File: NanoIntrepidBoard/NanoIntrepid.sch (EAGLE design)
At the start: 22 parts, among them Q1 TRANS_NPN, Q2 TRANS_NPN, Q3 TRANS_NPN, Q4 TRANS_PNP, Q5 TRANS_PNP, Q6 TRANS_PNP, U1 NANO, U2 MOSFET_P, U3 MOSFET_P, U4 MOSFET_P

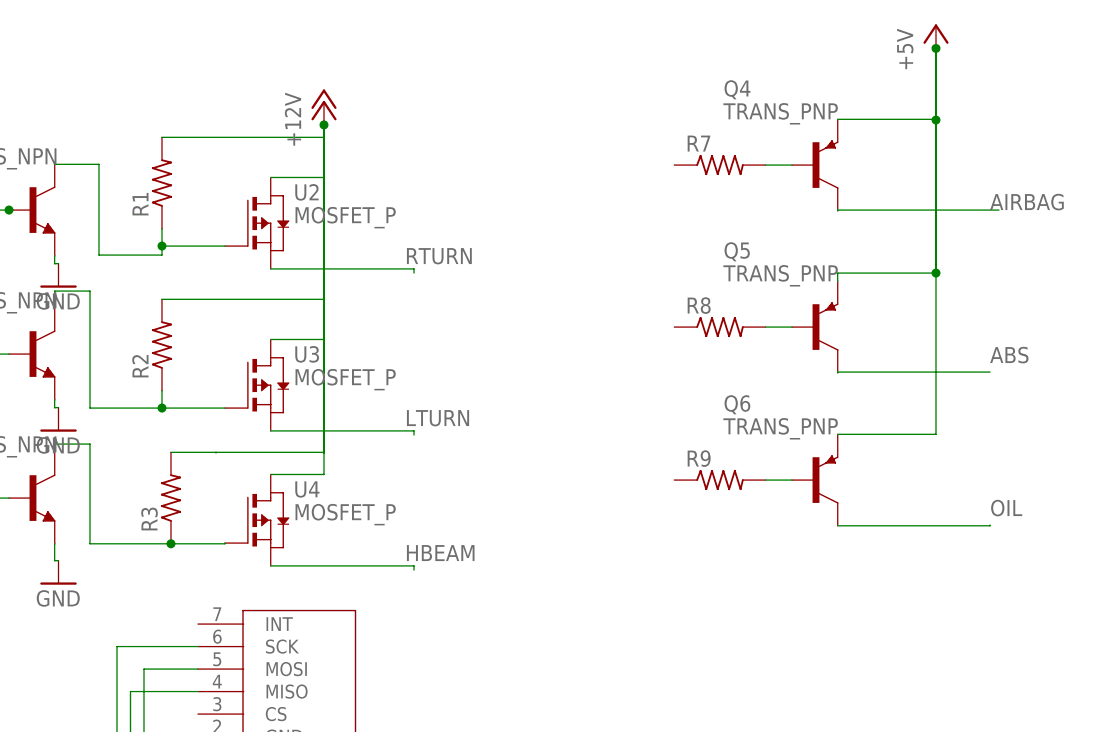
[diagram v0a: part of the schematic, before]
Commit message: Fixed some Eagle Library mistakes and started laying out board
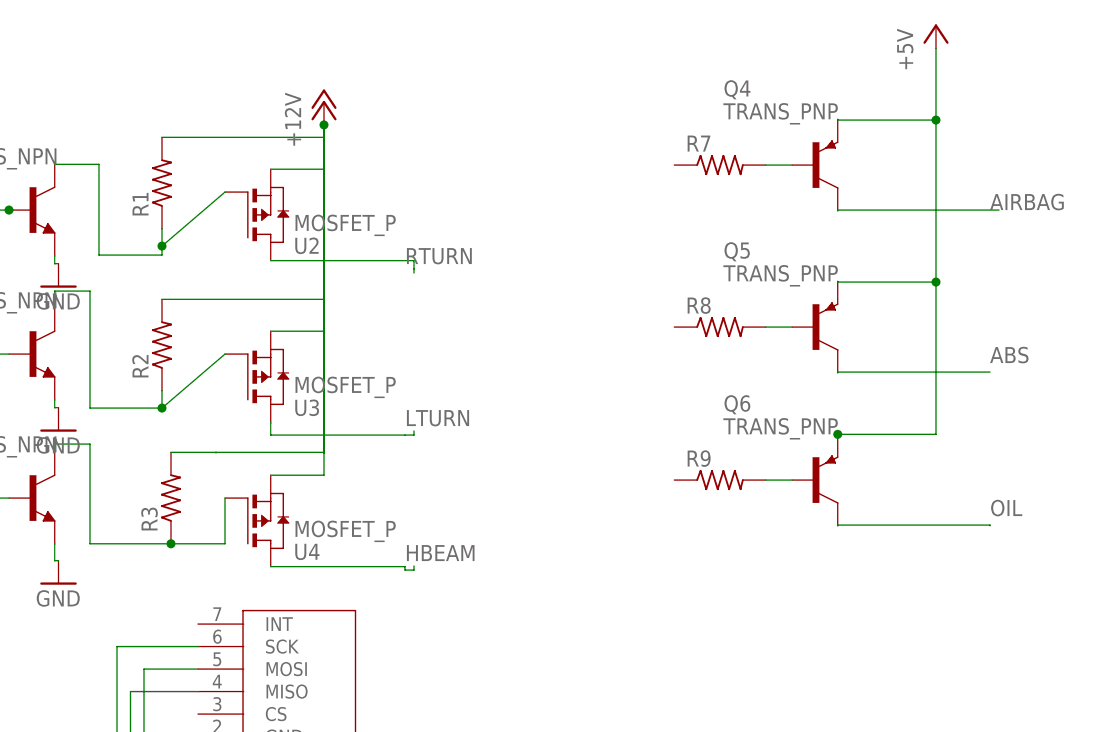
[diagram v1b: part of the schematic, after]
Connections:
- net +12V: now also U2.S, U3.S, U4.S; no longer U2.D, U3.D, U4.D
- net +5V: now also Q4.E, Q5.E, Q6.E; no longer Q4.C, Q5.C, Q6.C
- net ABS: now also Q5.C; no longer Q5.E
- net AIRBAG: now also Q4.C; no longer Q4.E
- net HBEAM: now also U4.D; no longer U4.S
- net LTURN: now also U3.D; no longer U3.S
- net OIL: now also Q6.C; no longer Q6.E
- net RTURN: now also U2.D; no longer U2.S
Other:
- moved on the sheet: U2, U3, U4
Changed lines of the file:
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@@
 <attribute name="VALUE" x="4.96" y="68.46" size="1.778" layer="96"/>
 </instance>
-<instance part="U2" gate="G$1" x="107" y="100" smashed="yes">
-<attribute name="VALUE" x="114.62" y="102.54" size="1.778" layer="96"/>
-<attribute name="NAME" x="114.62" y="105.08" size="1.778" layer="95"/>
-</instance>
-<instance part="U3" gate="G$1" x="107" y="82" smashed="yes">
-<attribute name="VALUE" x="114.62" y="84.54" size="1.778" layer="96"/>
-<attribute name="NAME" x="114.62" y="87.08" size="1.778" layer="95"/>
-</instance>
-<instance part="U4" gate="G$1" x="107" y="67" smashed="yes">
-<attribute name="VALUE" x="114.62" y="69.54" size="1.778" layer="96"/>
-<attribute name="NAME" x="114.62" y="72.08" size="1.778" layer="95"/>
+<instance part="U2" gate="G$1" x="107" y="106" smashed="yes" rot="MR180">
+<attribute name="VALUE" x="114.62" y="103.46" size="1.778" layer="96" rot="MR180"/>
+<attribute name="NAME" x="114.62" y="100.92" size="1.778" layer="95" rot="MR180"/>
+</instance>
+<instance part="U3" gate="G$1" x="107" y="88" smashed="yes" rot="MR180">
+<attribute name="VALUE" x="114.62" y="85.46" size="1.778" layer="96" rot="MR180"/>
+<attribute name="NAME" x="114.62" y="82.92" size="1.778" layer="95" rot="MR180"/>
+</instance>
+<instance part="U4" gate="G$1" x="107" y="72" smashed="yes" rot="MR180">
+<attribute name="VALUE" x="114.62" y="69.46" size="1.778" layer="96" rot="MR180"/>
+<attribute name="NAME" x="114.62" y="66.92" size="1.778" layer="95" rot="MR180"/>
 </instance>
 <instance part="R1" gate="G$1" x="100" y="107" smashed="yes" rot="R90">
@@
 <segment>
 <pinref part="P+5" gate="1" pin="+5V"/>
-<wire x1="186" y1="121.96" x2="186" y2="114.08" width="0.1524" layer="91"/>
-<pinref part="Q4" gate="G$1" pin="C"/>
-<wire x1="186" y1="114.08" x2="175.08" y2="114.08" width="0.1524" layer="91"/>
 <wire x1="186" y1="121.96" x2="186" y2="114" width="0.1524" layer="91"/>
-<junction x="186" y="121.96"/>
-<pinref part="Q5" gate="G$1" pin="C"/>
-<wire x1="186" y1="114" x2="186" y2="97" width="0.1524" layer="91"/>
-<wire x1="186" y1="97" x2="175.08" y2="97" width="0.1524" layer="91"/>
-<wire x1="175.08" y1="97" x2="175.08" y2="96.08" width="0.1524" layer="91"/>
-<pinref part="Q6" gate="G$1" pin="C"/>
-<wire x1="186" y1="121.96" x2="186" y2="114" width="0.1524" layer="91"/>
-<wire x1="186" y1="114" x2="186" y2="97" width="0.1524" layer="91"/>
-<wire x1="186" y1="97" x2="186" y2="79.08" width="0.1524" layer="91"/>
+<wire x1="186" y1="114" x2="186" y2="96" width="0.1524" layer="91"/>
+<junction x="186" y="114"/>
+<pinref part="Q4" gate="G$1" pin="E"/>
+<wire x1="186" y1="114" x2="175.08" y2="114" width="0.1524" layer="91"/>
+<wire x1="175.08" y1="114" x2="175.08" y2="114.08" width="0.1524" layer="91"/>
+<pinref part="Q5" gate="G$1" pin="E"/>
+<wire x1="186" y1="96" x2="175.08" y2="96" width="0.1524" layer="91"/>
+<wire x1="175.08" y1="96" x2="175.08" y2="96.08" width="0.1524" layer="91"/>
+<wire x1="186" y1="96" x2="186" y2="79.08" width="0.1524" layer="91"/>
+<junction x="186" y="96"/>
+<pinref part="Q6" gate="G$1" pin="E"/>
+<wire x1="175.08" y1="79" x2="175.08" y2="79.08" width="0.1524" layer="91"/>
 <wire x1="186" y1="79.08" x2="175.08" y2="79.08" width="0.1524" layer="91"/>
-<junction x="186" y="114"/>
-<junction x="186" y="97"/>
+<junction x="175.08" y="79.08"/>
 </segment>
 </net>
@@
 <wire x1="100" y1="112.08" x2="118" y2="112.08" width="0.1524" layer="91"/>
 <wire x1="118" y1="112.08" x2="118" y2="113.46" width="0.1524" layer="91"/>
-<pinref part="U2" gate="G$1" pin="D"/>
-<wire x1="112.08" y1="107.62" x2="118" y2="107.62" width="0.1524" layer="91"/>
 <wire x1="118" y1="107.62" x2="118" y2="113.46" width="0.1524" layer="91"/>
 <junction x="118" y="113.46"/>
@@
 <wire x1="100" y1="94.08" x2="118" y2="94.08" width="0.1524" layer="91"/>
 <wire x1="118" y1="94.08" x2="118" y2="113.46" width="0.1524" layer="91"/>
-<pinref part="U3" gate="G$1" pin="D"/>
-<wire x1="118" y1="113.46" x2="118" y2="89.62" width="0.1524" layer="91"/>
-<wire x1="118" y1="89.62" x2="112.08" y2="89.62" width="0.1524" layer="91"/>
-<pinref part="U4" gate="G$1" pin="D"/>
-<wire x1="112.08" y1="74.62" x2="118" y2="74.62" width="0.1524" layer="91"/>
-<wire x1="118" y1="74.62" x2="118" y2="113.46" width="0.1524" layer="91"/>
 <pinref part="R3" gate="G$1" pin="2"/>
+<wire x1="118" y1="74.54" x2="118" y2="77.08" width="0.1524" layer="91"/>
 <wire x1="101" y1="77.08" x2="118" y2="77.08" width="0.1524" layer="91"/>
-<wire x1="118" y1="77.08" x2="118" y2="113.46" width="0.1524" layer="91"/>
+<wire x1="118" y1="77.08" x2="118" y2="90.54" width="0.1524" layer="91"/>
+<pinref part="U4" gate="G$1" pin="S"/>
+<wire x1="118" y1="90.54" x2="118" y2="113.46" width="0.1524" layer="91"/>
+<wire x1="118" y1="74.54" x2="112.08" y2="74.54" width="0.1524" layer="91"/>
+<pinref part="U3" gate="G$1" pin="S"/>
+<wire x1="118" y1="90.54" x2="112.08" y2="90.54" width="0.1524" layer="91"/>
+<pinref part="U2" gate="G$1" pin="S"/>
+<wire x1="112.08" y1="108.54" x2="118" y2="108.54" width="0.1524" layer="91"/>
+<wire x1="118" y1="108.54" x2="118" y2="113.46" width="0.1524" layer="91"/>
 </segment>
 </net>
@@
 <pinref part="U2" gate="G$1" pin="G"/>
 <pinref part="R1" gate="G$1" pin="1"/>
-<wire x1="107" y1="100" x2="100" y2="100" width="0.1524" layer="91"/>
+<wire x1="107" y1="106" x2="100" y2="100" width="0.1524" layer="91"/>
 <wire x1="100" y1="100" x2="100" y2="101.92" width="0.1524" layer="91"/>
 <wire x1="100" y1="100" x2="100" y2="99" width="0.1524" layer="91"/>
@@
 <segment>
 <pinref part="U3" gate="G$1" pin="G"/>
-<wire x1="107" y1="82" x2="100" y2="82" width="0.1524" layer="91"/>
+<wire x1="107" y1="88" x2="100" y2="82" width="0.1524" layer="91"/>
 <pinref part="R2" gate="G$1" pin="1"/>
 <wire x1="100" y1="82" x2="100" y2="83.92" width="0.1524" layer="91"/>
@@
 <pinref part="U4" gate="G$1" pin="G"/>
 <pinref part="R3" gate="G$1" pin="1"/>
-<wire x1="107" y1="67" x2="107" y2="66.92" width="0.1524" layer="91"/>
+<wire x1="107" y1="72" x2="107" y2="66.92" width="0.1524" layer="91"/>
 <wire x1="107" y1="66.92" x2="101" y2="66.92" width="0.1524" layer="91"/>
 <wire x1="101" y1="66.92" x2="92" y2="66.92" width="0.1524" layer="91"/>
@@
 <net name="RTURN" class="0">
 <segment>
-<pinref part="U2" gate="G$1" pin="S"/>
-<wire x1="112.08" y1="97.46" x2="128" y2="97.46" width="0.1524" layer="91"/>
 <wire x1="128" y1="97.46" x2="128" y2="97" width="0.1524" layer="91"/>
 <label x="127" y="98" size="1.778" layer="95"/>
+<pinref part="U2" gate="G$1" pin="D"/>
+<wire x1="112.08" y1="98.38" x2="128" y2="98.38" width="0.1524" layer="91"/>
+<wire x1="128" y1="98.38" x2="128" y2="97.46" width="0.1524" layer="91"/>
 </segment>
 </net>
 <net name="LTURN" class="0">
 <segment>
-<pinref part="U3" gate="G$1" pin="S"/>
-<wire x1="112.08" y1="79.46" x2="128" y2="79.46" width="0.1524" layer="91"/>
 <wire x1="128" y1="79.46" x2="128" y2="79" width="0.1524" layer="91"/>
 <label x="127" y="80" size="1.778" layer="95"/>
+<pinref part="U3" gate="G$1" pin="D"/>
+<wire x1="112.08" y1="80.38" x2="112.08" y2="79" width="0.1524" layer="91"/>
+<wire x1="112.08" y1="79" x2="127" y2="79" width="0.1524" layer="91"/>
+<wire x1="128" y1="79" x2="127" y2="79" width="0.1524" layer="91"/>
 </segment>
 </net>
 <net name="HBEAM" class="0">
 <segment>
-<pinref part="U4" gate="G$1" pin="S"/>
-<wire x1="112.08" y1="64.46" x2="128" y2="64.46" width="0.1524" layer="91"/>
 <wire x1="128" y1="64.46" x2="128" y2="64" width="0.1524" layer="91"/>
 <label x="127" y="65" size="1.778" layer="95"/>
+<pinref part="U4" gate="G$1" pin="D"/>
+<wire x1="112.08" y1="64.38" x2="127" y2="64.38" width="0.1524" layer="91"/>
+<wire x1="127" y1="64.38" x2="127" y2="64" width="0.1524" layer="91"/>
+<wire x1="128" y1="64" x2="127" y2="64" width="0.1524" layer="91"/>
 </segment>
 </net>
@@
 <net name="AIRBAG" class="0">
 <segment>
-<pinref part="Q4" gate="G$1" pin="E"/>
-<wire x1="175.08" y1="103.92" x2="175.08" y2="104" width="0.1524" layer="91"/>
-<wire x1="175.08" y1="104" x2="193" y2="104" width="0.1524" layer="91"/>
 <label x="192" y="104" size="1.778" layer="95"/>
+<pinref part="Q4" gate="G$1" pin="C"/>
+<wire x1="193" y1="104" x2="175.08" y2="104" width="0.1524" layer="91"/>
+<wire x1="175.08" y1="104" x2="175.08" y2="103.92" width="0.1524" layer="91"/>
 </segment>
 </net>
 <net name="ABS" class="0">
 <segment>
-<pinref part="Q5" gate="G$1" pin="E"/>
-<wire x1="175.08" y1="85.92" x2="175.08" y2="86" width="0.1524" layer="91"/>
-<wire x1="175.08" y1="86" x2="192" y2="86" width="0.1524" layer="91"/>
 <label x="192" y="87" size="1.778" layer="95"/>
+<pinref part="Q5" gate="G$1" pin="C"/>
+<wire x1="192" y1="86" x2="175.08" y2="86" width="0.1524" layer="91"/>
+<wire x1="175.08" y1="86" x2="175.08" y2="85.92" width="0.1524" layer="91"/>
 </segment>
 </net>
 <net name="OIL" class="0">
 <segment>
-<pinref part="Q6" gate="G$1" pin="E"/>
-<wire x1="175.08" y1="68.92" x2="192" y2="68.92" width="0.1524" layer="91"/>
 <wire x1="192" y1="68.92" x2="192" y2="69" width="0.1524" layer="91"/>
 <label x="192" y="70" size="1.778" layer="95"/>
-</segment>
-</net>
+<pinref part="Q6" gate="G$1" pin="C"/>
+<wire x1="192" y1="69" x2="175.08" y2="69" width="0.1524" layer="91"/>
+<wire x1="175.08" y1="69" x2="175.08" y2="68.92" width="0.1524" layer="91"/>
+</segment>
+</net>

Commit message: Worked on board files
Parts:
- added JP3: (no value), pinhead:PINHD-1X1
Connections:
- new net ABS_UC: R8.1, U1.A4
- new net AIRBAG_UC: R7.1, U1.A5
- new net HB_UC: R4.1, U1.A2
- new net LTURN_UC: R6.1, U1.A0
- new net OIL_UC: R9.1, U1.A3
- new net PB: JP3.1, U1.D3
- new net RTURN_UC: R5.1, U1.A1
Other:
- moved on the sheet: R4, R5, R6, R7, R8, R9
